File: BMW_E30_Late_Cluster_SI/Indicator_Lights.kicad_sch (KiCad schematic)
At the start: 34 parts, among them J1 SI LED Board, Q19 BC337-25, Q21 BC337-25, Q22 BC337-25, Q23 BC337-25, U4 ITT SAF1194-280 MCU, Y2 Crystal

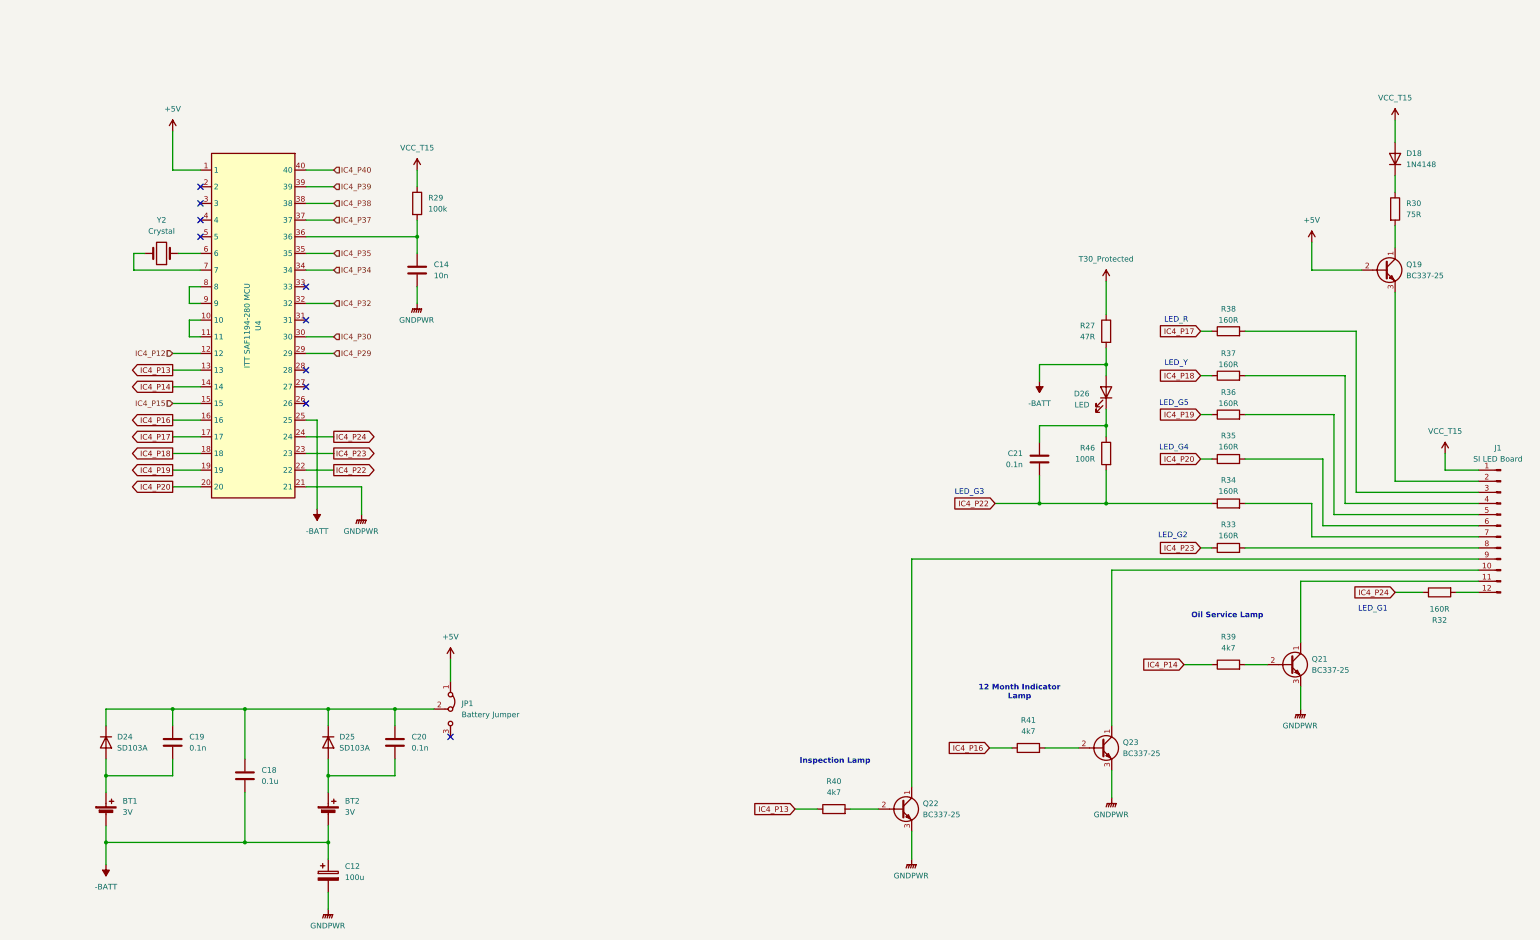
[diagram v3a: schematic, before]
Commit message: SI layout updates
Component positions are mostly complete.
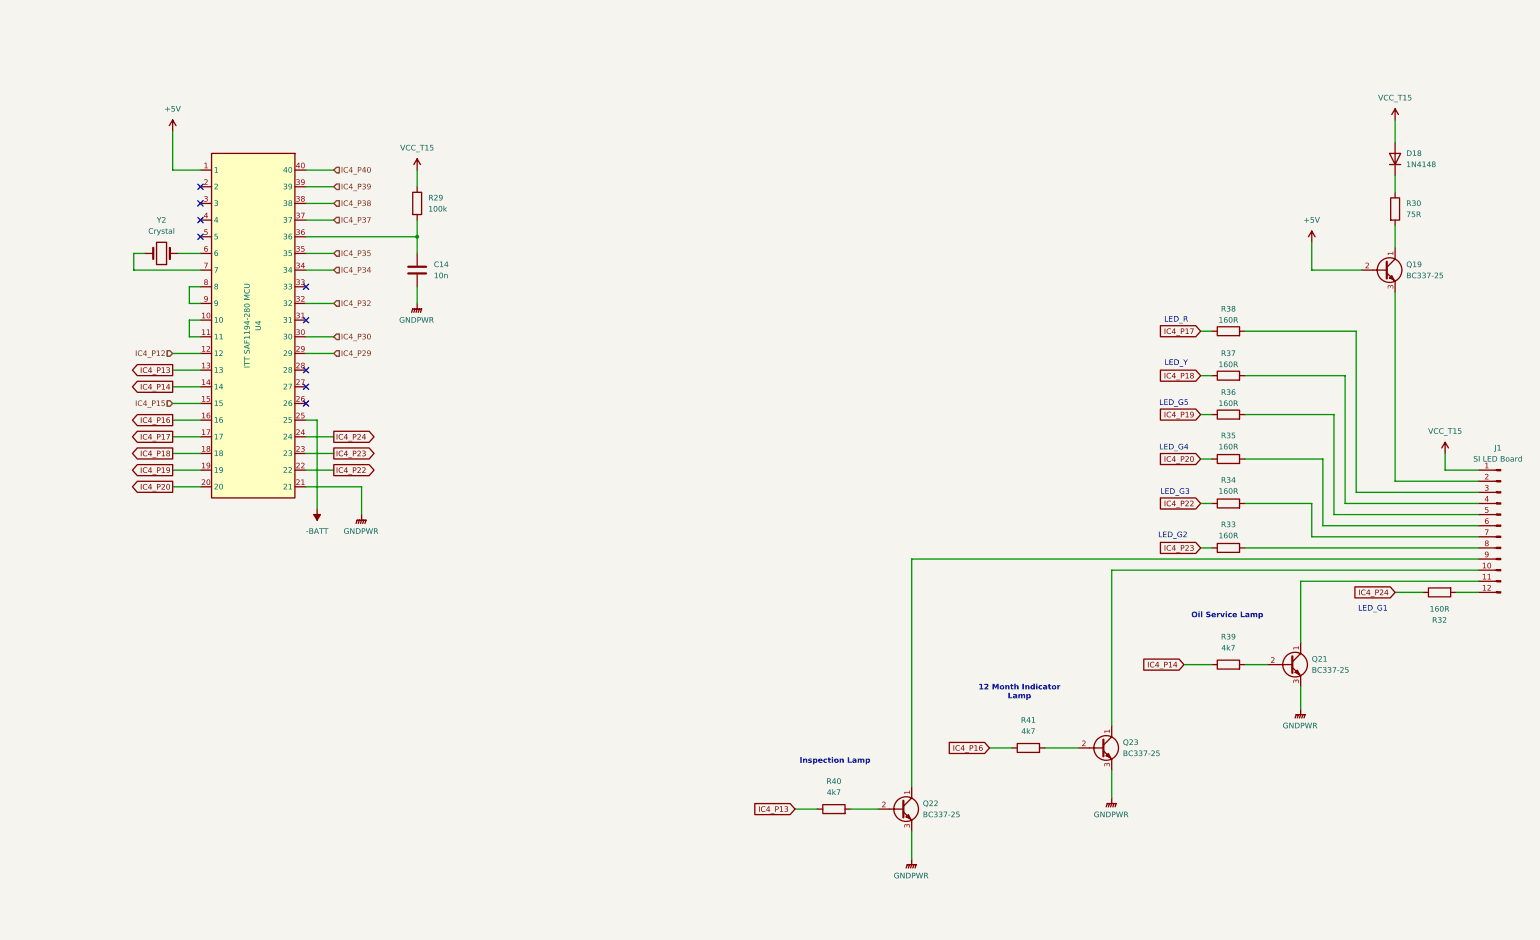
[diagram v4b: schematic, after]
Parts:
- removed BT1, BT2: 3V, symbol Device:Battery_Cell
- removed C12: 100u, Capacitor_THT:CP_Axial_L18.0mm_D6.5mm_P25.00mm_Horizontal, symbol Device:C_Polarized
- removed C18: 0.1u, Capacitor_THT:C_Rect_L7.0mm_W2.0mm_P5.00mm, symbol Device:C
- removed C19, C20, C21: 0.1n, Capacitor_THT:C_Disc_D6.0mm_W2.5mm_P5.00mm, symbol Device:C
- removed D24, D25: SD103A, symbol Device:D
- removed D26: LED, symbol Device:LED
- removed JP1: Battery Jumper, symbol Jumper:Jumper_3_Bridged12
- removed R27: 47R, Resistor_THT:R_Axial_DIN0516_L15.5mm_D5.0mm_P20.32mm_Horizontal, symbol Device:R
- removed R46: 100R, SI_THT:R_Axial_Narrow_L6.8mm_D2.4mm_P9.7mm, symbol Device:R
- D18: footprint (none) -> SI_THT:D_Axial_Narrow_L6.7mm_D2.4mm_P9.7mm
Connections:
- no-connect marks 10 -> 9

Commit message: SI Board Layout Complete
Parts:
- added JP1: Jumper, SI_THT:Jumper_THT_P9.7mm, symbol Jumper:Jumper_2_Bridged
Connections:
- net at C14.1, R29.2: now also JP1.2 (B); no longer U4.36
- new net: JP1.1 (A), U4.36
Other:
- moved on the sheet: C14, R29
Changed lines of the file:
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@@
 	)
 	(junction
-		(at 115.57 66.04)
+		(at 129.54 66.04)
 		(diameter 0)
 		(color 0 0 0 0)
@@
 	(wire
 		(pts
-			(xy 115.57 50.8) (xy 115.57 54.61)
+			(xy 129.54 50.8) (xy 129.54 54.61)
 		)
 		(stroke
@@
 	(wire
 		(pts
-			(xy 115.57 77.47) (xy 115.57 81.28)
+			(xy 129.54 77.47) (xy 129.54 81.28)
 		)
 		(stroke
@@
 	(wire
 		(pts
+			(xy 90.17 66.04) (xy 107.95 66.04)
+		)
+		(stroke
+			(width 0)
+			(type default)
+		)
+	)
+	(wire
+		(pts
 			(xy 66.04 85.09) (xy 63.5 85.09)
 		)
@@
 	(wire
 		(pts
-			(xy 90.17 66.04) (xy 115.57 66.04)
+			(xy 339.09 78.74) (xy 339.09 121.92)
 		)
 		(stroke
@@
 	(wire
 		(pts
-			(xy 339.09 78.74) (xy 339.09 121.92)
+			(xy 320.04 134.62) (xy 358.14 134.62)
 		)
 		(stroke
@@
 	(wire
 		(pts
-			(xy 320.04 134.62) (xy 358.14 134.62)
+			(xy 294.64 106.68) (xy 297.18 106.68)
 		)
 		(stroke
@@
 	(wire
 		(pts
-			(xy 294.64 106.68) (xy 297.18 106.68)
+			(xy 118.11 66.04) (xy 129.54 66.04)
 		)
 		(stroke
@@
 	(wire
 		(pts
-			(xy 115.57 66.04) (xy 115.57 69.85)
+			(xy 129.54 62.23) (xy 129.54 66.04)
 		)
 		(stroke
@@
 	(wire
 		(pts
-			(xy 115.57 62.23) (xy 115.57 66.04)
+			(xy 129.54 66.04) (xy 129.54 69.85)
 		)
 		(stroke
@@
 	)
 	(symbol
+		(lib_id "Jumper:Jumper_2_Bridged")
+		(at 113.03 66.04 0)
+		(unit 1)
+		(exclude_from_sim no)
+		(in_bom yes)
+		(on_board yes)
+		(dnp no)
+		(fields_autoplaced yes)
+		(property "Reference" "JP1"
+			(at 113.03 60.96 0)
+			(effects
+				(font
+					(size 1.27 1.27)
+				)
+			)
+		)
+		(property "Value" "Jumper"
+			(at 113.03 63.5 0)
+			(effects
+				(font
+					(size 1.27 1.27)
+				)
+			)
+		)
+		(property "Footprint" "SI_THT:Jumper_THT_P9.7mm"
+			(at 113.03 66.04 0)
+			(effects
+				(font
+					(size 1.27 1.27)
+				)
+				(hide yes)
+			)
+		)
+		(property "Datasheet" "~"
+			(at 113.03 66.04 0)
+			(effects
+				(font
+					(size 1.27 1.27)
+				)
+				(hide yes)
+			)
+		)
+		(property "Description" "Jumper, 2-pole, closed/bridged"
+			(at 113.03 66.04 0)
+			(effects
+				(font
+					(size 1.27 1.27)
+				)
+				(hide yes)
+			)
+		)
+		(pin "2"
+		)
+		(pin "1"
+		)
+		(instances
+			(project "BMW_E30_Late_Cluster_SI"
+				(path "/00d578f4-1582-4e4e-9a07-e5462d38fb61/b04c7dca-233f-4936-a882-7f55988b8ad8"
+					(reference "JP1")
+					(unit 1)
+				)
+			)
+		)
+	)
+	(symbol
 		(lib_id "Device:R")
 		(at 300.99 97.79 90)
@@
 	(symbol
 		(lib_id "power:+12V")
-		(at 115.57 50.8 0)
+		(at 129.54 50.8 0)
 		(unit 1)
 		(exclude_from_sim no)
@@
 		(fields_autoplaced yes)
 		(property "Reference" "#PWR012"
-			(at 115.57 54.61 0)
+			(at 129.54 54.61 0)
 			(effects
 				(font
@@
 		)
 		(property "Value" "VCC_T15"
-			(at 115.57 45.72 0)
+			(at 129.54 45.72 0)
 			(effects
 				(font
@@
 		)
 		(property "Footprint" ""
-			(at 115.57 50.8 0)
+			(at 129.54 50.8 0)
 			(effects
 				(font
@@
 		)
 		(property "Datasheet" ""
-			(at 115.57 50.8 0)
+			(at 129.54 50.8 0)
 			(effects
 				(font
@@
 		)
 		(property "Description" "Power symbol creates a global label with name \"+12V\""
-			(at 115.57 50.8 0)
+			(at 129.54 50.8 0)
 			(effects
 				(font
@@
 	(symbol
 		(lib_id "Device:C")
-		(at 115.57 73.66 0)
+		(at 129.54 73.66 0)
 		(unit 1)
 		(exclude_from_sim no)
@@
 		(fields_autoplaced yes)
 		(property "Reference" "C14"
-			(at 119.38 72.3899 0)
+			(at 133.35 72.3899 0)
 			(effects
 				(font
@@
 		)
 		(property "Value" "10n"
-			(at 119.38 74.9299 0)
+			(at 133.35 74.9299 0)
 			(effects
 				(font
@@
 		)
 		(property "Footprint" "Capacitor_THT:C_Disc_D6.0mm_W2.5mm_P5.00mm"
-			(at 116.5352 77.47 0)
+			(at 130.5052 77.47 0)
 			(effects
 				(font
@@
 		)
 		(property "Datasheet" "~"
-			(at 115.57 73.66 0)
+			(at 129.54 73.66 0)
 			(effects
 				(font
@@
 		)
 		(property "Description" "Unpolarized capacitor"
-			(at 115.57 73.66 0)
+			(at 129.54 73.66 0)
 			(effects
 				(font
@@
 	(symbol
 		(lib_id "Device:R")
-		(at 115.57 58.42 0)
+		(at 129.54 58.42 0)
 		(unit 1)
 		(exclude_from_sim no)
@@
 		(fields_autoplaced yes)
 		(property "Reference" "R29"
-			(at 118.11 57.1499 0)
+			(at 132.08 57.1499 0)
 			(effects
 				(font
@@
 		)
 		(property "Value" "100k"
-			(at 118.11 59.6899 0)
+			(at 132.08 59.6899 0)
 			(effects
 				(font
@@
 		)
 		(property "Footprint" "SI_THT:R_Axial_Narrow_L6.8mm_D2.4mm_P9.7mm"
-			(at 113.792 58.42 90)
+			(at 127.762 58.42 90)
 			(effects
 				(font
@@
 		)
 		(property "Datasheet" "~"
-			(at 115.57 58.42 0)
+			(at 129.54 58.42 0)
 			(effects
 				(font
@@
 		)
 		(property "Description" "5%"
-			(at 115.57 58.42 0)
+			(at 129.54 58.42 0)
 			(effects
 				(font
@@
 	(symbol
 		(lib_id "power:GNDPWR")
-		(at 115.57 81.28 0)
+		(at 129.54 81.28 0)
 		(unit 1)
 		(exclude_from_sim no)
@@
 		(fields_autoplaced yes)
 		(property "Reference" "#PWR026"
-			(at 115.57 86.36 0)
+			(at 129.54 86.36 0)
 			(effects
 				(font
@@
 		)
 		(property "Value" "GNDPWR"
-			(at 115.443 85.09 0)
+			(at 129.413 85.09 0)
 			(effects
 				(font
@@
 		)
 		(property "Footprint" ""
-			(at 115.57 82.55 0)
+			(at 129.54 82.55 0)
 			(effects
 				(font
@@
 		)
 		(property "Datasheet" ""
-			(at 115.57 82.55 0)
+			(at 129.54 82.55 0)
 			(effects
 				(font
@@
 		)
 		(property "Description" "Power symbol creates a global label with name \"GNDPWR\" , global ground"
-			(at 115.57 81.28 0)
+			(at 129.54 81.28 0)
 			(effects
 				(font

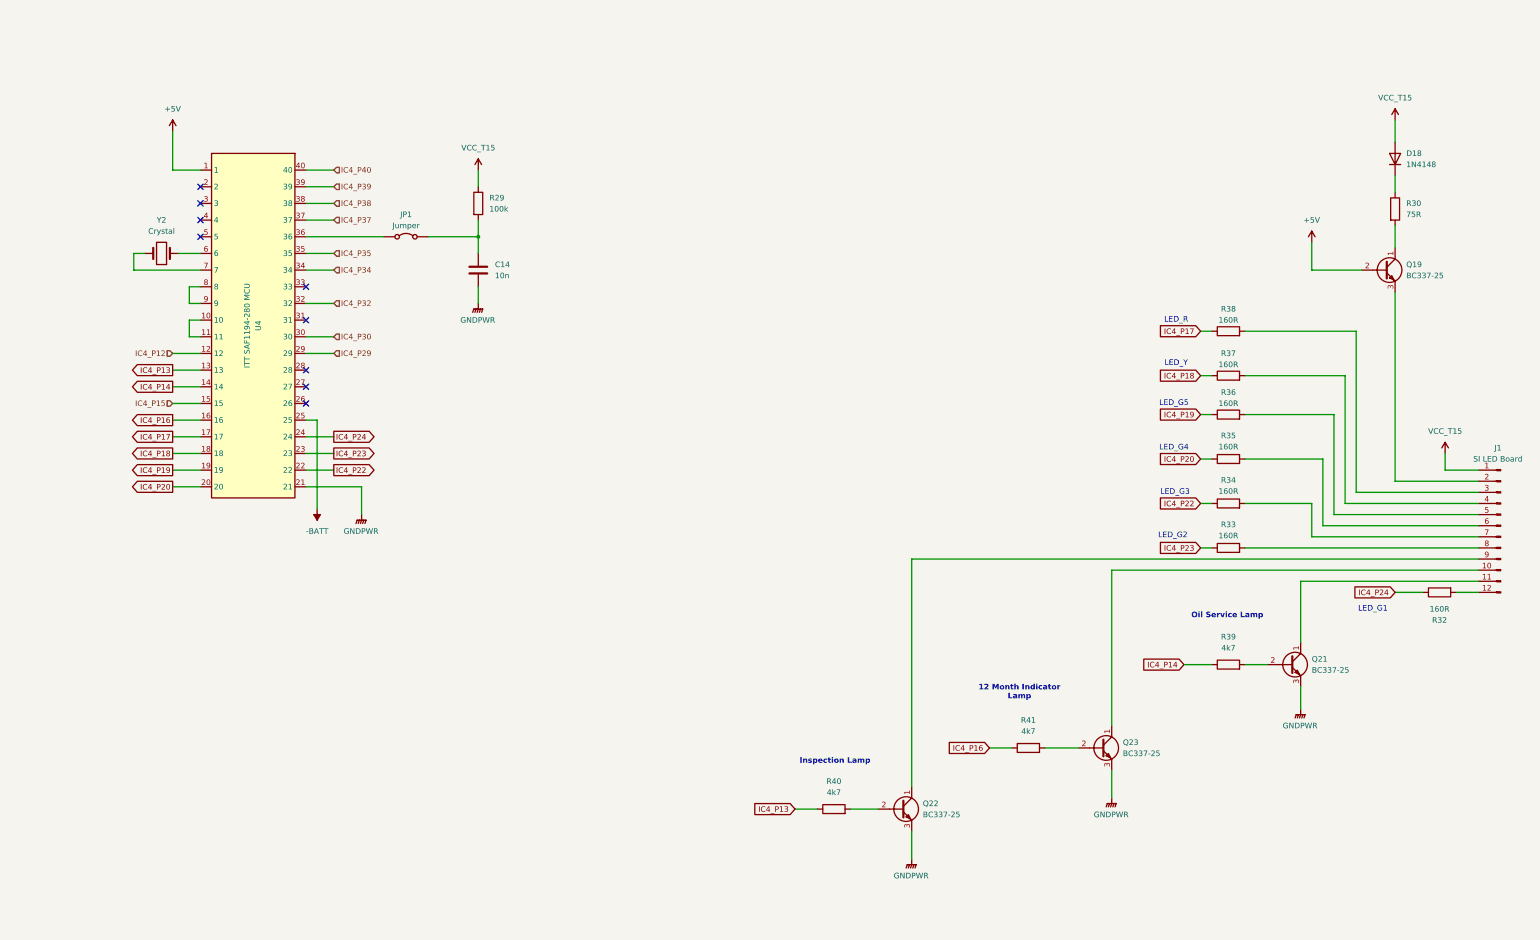
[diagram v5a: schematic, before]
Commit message: Readability Improvements
Organized the schematic for better readability, also made a few minor adjustments to the layout for simplicity.
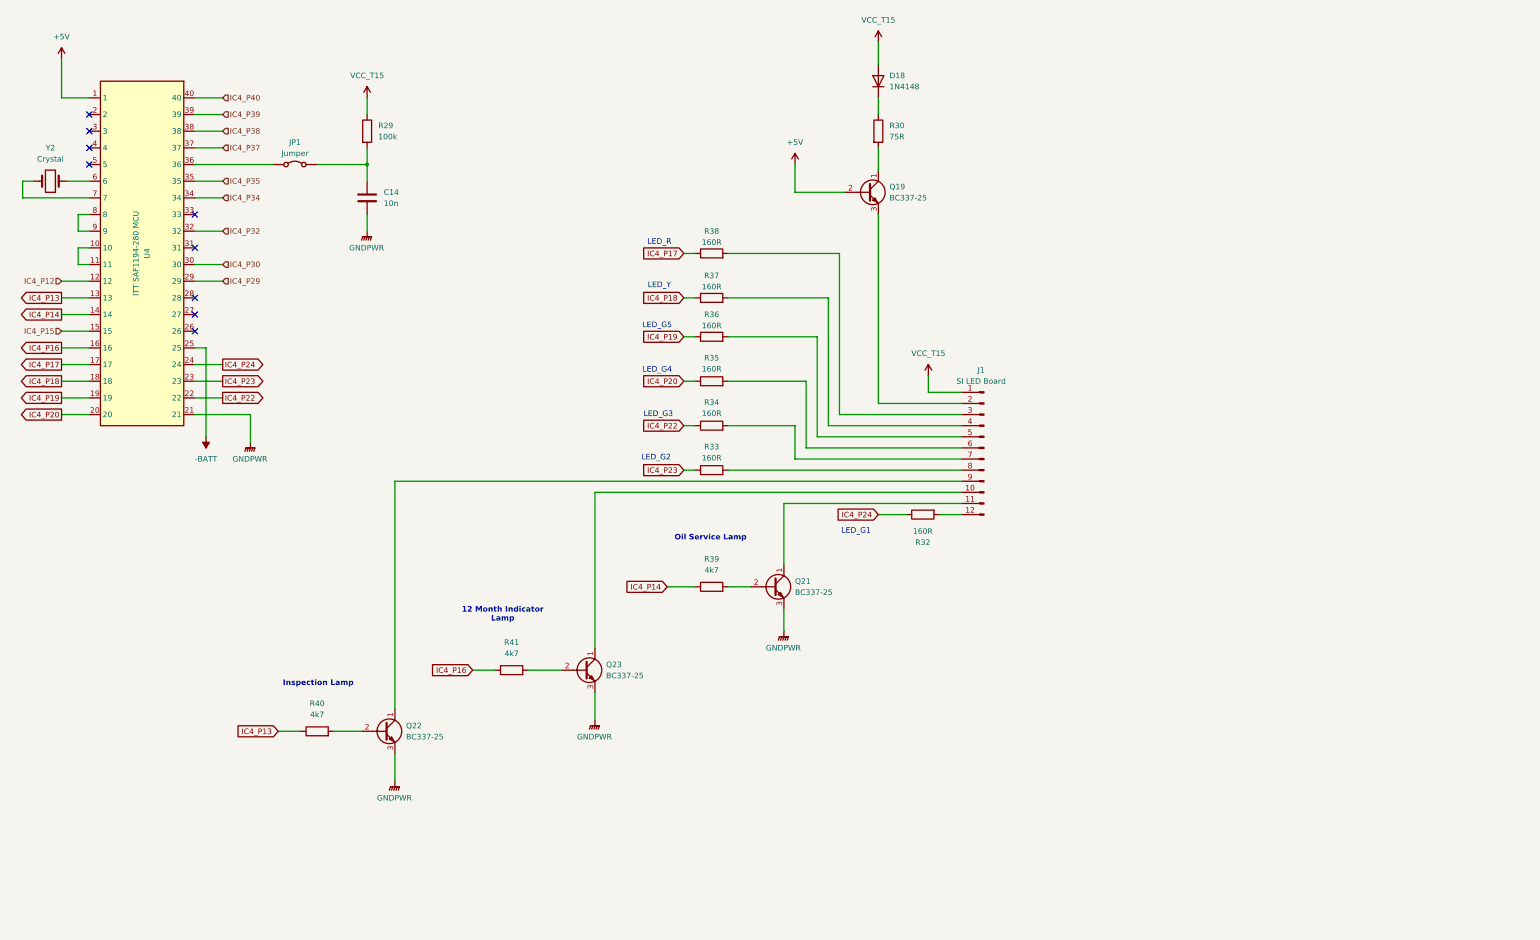
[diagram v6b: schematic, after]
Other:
- moved on the sheet: C14, D18, J1, JP1, Q19, Q21, Q22, Q23, R29, R30, R32, R33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

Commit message: Layout Updates
Moved battery footprints to closer match the original. Also moved the groupings of resistors in the center lower section of the board to be further away from the board edge for better fitment.
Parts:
- J1: footprint Connector_PinHeader_2.54mm:PinHeader_1x12_P2.54mm_Vertical -> BMW_Cluster_Connectors:SILight_1x12_P2.54mm_Vertical_PinHeader
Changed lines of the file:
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@@
 			)
 		)
-		(property "Footprint" "Connector_PinHeader_2.54mm:PinHeader_1x12_P2.54mm_Vertical"
+		(property "Footprint" "BMW_Cluster_Connectors:SILight_1x12_P2.54mm_Vertical_PinHeader"
 			(at 245.11 114.3 0)
 			(effects
